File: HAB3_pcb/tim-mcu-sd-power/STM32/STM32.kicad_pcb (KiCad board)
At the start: 4 copper layers, 40 parts, among them J1 Conn_ARM_JTAG_SWD_20, J2 Micro_SD_Card_Det, J3 Conn_01x16_Male, J4 Conn_01x16_Male, J5 Conn_01x16_Male, J6 Conn_01x02_Male, J7 Conn_01x02_Male, J8 Conn_01x02_Male, J9 Conn_01x11_Male, SW1 SW_DPST_x2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

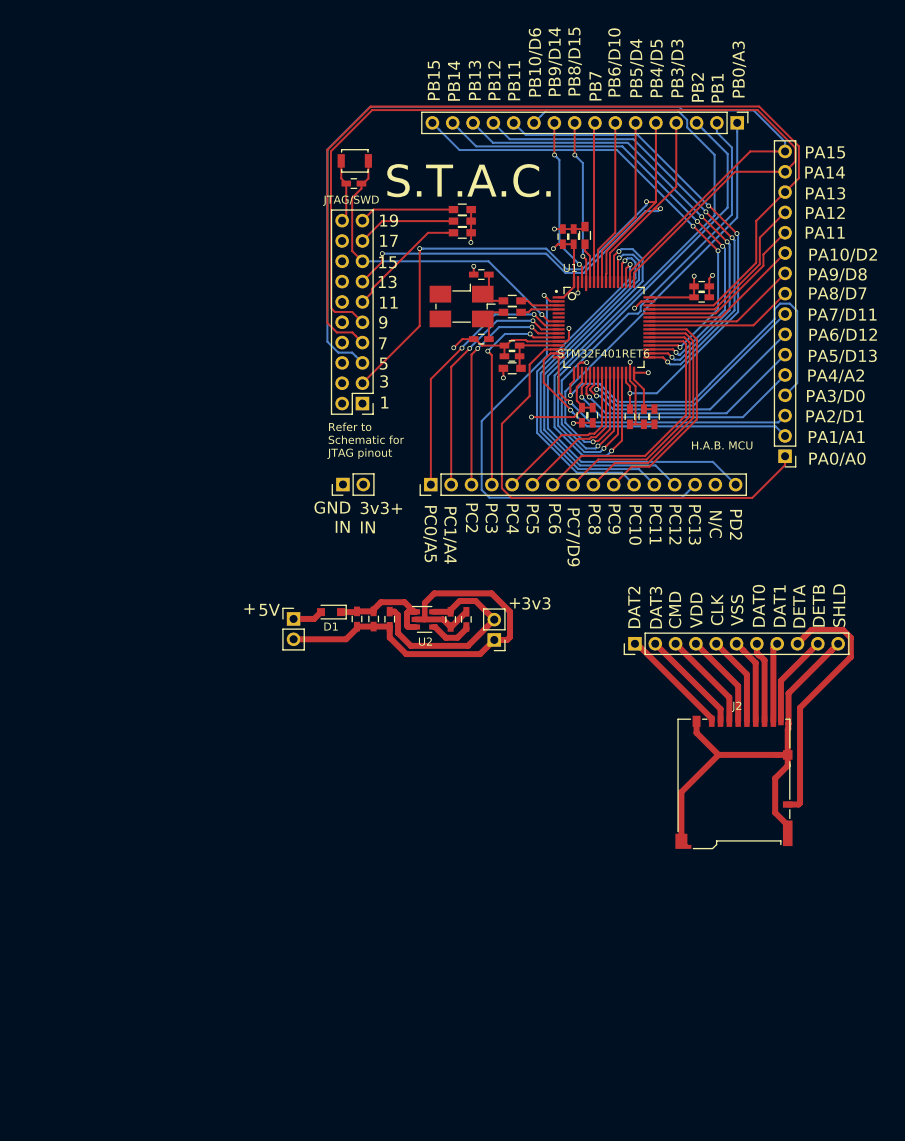
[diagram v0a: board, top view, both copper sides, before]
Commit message: Finished voltage regulator
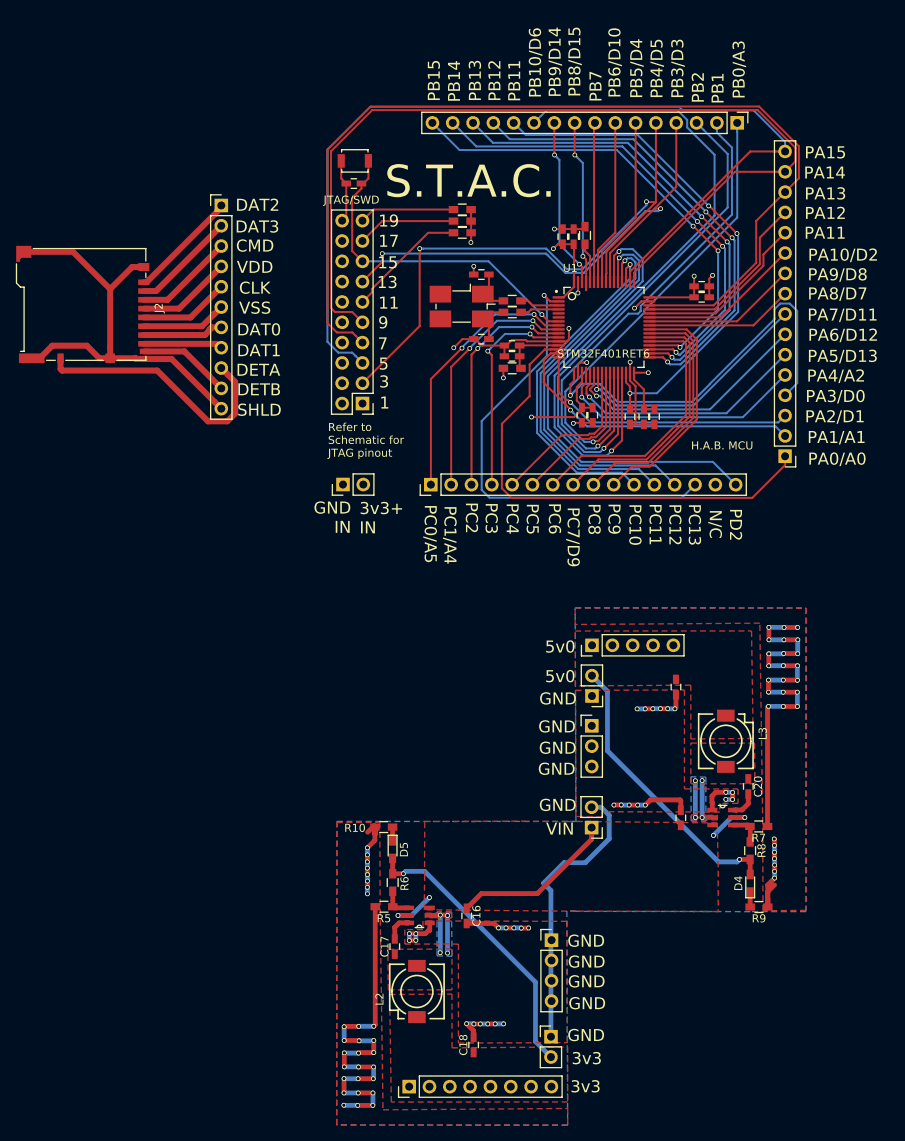
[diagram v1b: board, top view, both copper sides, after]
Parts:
- removed 100nF6: C17, Capacitors_SMD:C_0603_HandSoldering
- removed 100nF7: C20, Capacitors_SMD:C_0603_HandSoldering
- removed 10nF2: C18, Capacitors_SMD:C_0603_HandSoldering
- removed 1uF6: C16, Capacitors_SMD:C_0603_HandSoldering
- removed 1uF7: C19, Capacitors_SMD:C_0603_HandSoldering
- removed D1: D_Schottky, Diodes_SMD:D_SOD-323_HandSoldering
- added C16: 10uF, Capacitors_SMD:C_0603_HandSoldering, F.Cu at (131.3, 178.6)
- added C17: 100nF, Capacitors_SMD:C_0603_HandSoldering, F.Cu at (122.3, 182.4)
- added C18: 47uF, Capacitors_SMD:C_0603_HandSoldering, F.Cu at (132.2, 194.7)
- added C19: 10uF, Capacitors_SMD:C_0603_HandSoldering, F.Cu at (158.1, 166.3)
- added C20: 100nF, Capacitors_SMD:C_0603_HandSoldering, F.Cu at (166.5, 162.4)
- added C21: 47uF, Capacitors_SMD:C_0603_HandSoldering, F.Cu at (157.5, 150.0)
- added D4: LED, LEDs:LED_0603_HandSoldering, F.Cu at (166.8, 174.5)
- added D5: LED, LEDs:LED_0603_HandSoldering, F.Cu at (122.1, 170.3)
- added J10: Conn_01x02_Male, Pin_Headers:Pin_Header_Straight_1x02_Pitch2.54mm, F.Cu at (147.0, 151.1)
- added J12: Conn_01x03_Male, Pin_Headers:Pin_Header_Straight_1x03_Pitch2.54mm, F.Cu at (147.0, 154.8)
- added J13: Conn_01x04_Male, Pin_Headers:Pin_Header_Straight_1x04_Pitch2.54mm, F.Cu at (141.9, 181.6)
- added J14: Conn_01x05_Male, Pin_Headers:Pin_Header_Straight_1x05_Pitch2.54mm, F.Cu at (147.0, 144.7)
- added J15: Conn_01x08_Male, Pin_Headers:Pin_Header_Straight_1x08_Pitch2.54mm, F.Cu at (124.1, 199.9)
- added L2: 2.2uH, TPS564208:INDC7070X450, F.Cu at (125.0, 188.0)
- added L3: 3.3uH, TPS564208:INDC7070X450, F.Cu at (163.8, 156.8)
- added R10: 4.7k, Resistors_SMD:R_0603_HandSoldering, F.Cu at (121.0, 167.5)
- added R5: 10k, Resistors_SMD:R_0603_HandSoldering, F.Cu at (121.0, 177.4)
- added R6: 33.2k, Resistors_SMD:R_0603_HandSoldering, F.Cu at (122.1, 174.4)
- added R7: 10k, Resistors_SMD:R_0603_HandSoldering, F.Cu at (167.8, 167.4)
- added R8: 56.2k, Resistors_SMD:R_0603_HandSoldering, F.Cu at (166.8, 170.4)
- added R9: 4.7k, Resistors_SMD:R_0603_HandSoldering, F.Cu at (167.9, 177.5)
- added U3: TPS564208, TPS564208:TPS564208, F.Cu at (163.3, 166.3)
- 22uH1: value L -> L1
- U2: value LD3985M33R_SOT23 -> TPS564208; footprint TO_SOT_Packages_SMD:SOT-23-5 -> TPS564208:TPS564208
- moved J2 90.7 mm to (90.3, 99.4), turned to 270 degrees
- moved J9 75.3 mm to (100.7, 89.8), turned to 0 degrees
- moved J8 50.1 mm to (141.9, 193.7), turned to 0 degrees
- moved J7 45.5 mm to (147.0, 167.5), turned to 180 degrees
- moved U2 37.0 mm to (125.4, 178.5), turned to 180 degrees
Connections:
- J7 pad 1: Net-(D1-Pad2) -> Net-(C16-Pad1)
- J7 pad 2: Net-(100nF6-Pad1) -> Net-(C16-Pad2)
- J8 pad 1: Net-(100nF6-Pad1) -> Net-(C16-Pad2)
- J8 pad 2: Net-(100nF7-Pad2) -> Net-(C18-Pad1)
- U2 pad 1: Net-(100nF6-Pad2) -> Net-(C16-Pad2)
- U2 pad 2: Net-(100nF6-Pad1) -> Net-(C17-Pad1)
- U2 pad 3: Net-(100nF6-Pad2) -> Net-(C16-Pad1)
- U2 pad 5: Net-(100nF7-Pad2) -> Net-(C16-Pad1)
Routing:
- net Net-(C16-Pad2): track 0.00 -> 206.2 mm, vias 0 -> 87
- net Net-(100nF6-Pad1): track 56.0 -> 0.00 mm
- net Net-(C21-Pad1): track 0.00 -> 35.8 mm, vias 0 -> 1
- net Net-(C18-Pad1): track 0.00 -> 35.8 mm, vias 0 -> 1
- net Net-(C16-Pad1): track 0.00 -> 33.3 mm, vias 0 -> 4
- net Net-(100nF7-Pad2): track 26.8 -> 0.00 mm
- net Net-(100nF6-Pad2): track 14.4 -> 0.00 mm
- net Net-(C17-Pad1): track 0.00 -> 11.7 mm, vias 0 -> 4
- net Net-(C20-Pad1): track 0.00 -> 11.3 mm, vias 0 -> 4
- net Net-(R7-Pad2): track 0.00 -> 4.07 mm
- net Net-(C17-Pad2): track 0.00 -> 3.83 mm
- net Net-(D1-Pad2): track 3.78 -> 0.00 mm
- net Net-(C20-Pad2): track 0.00 -> 3.43 mm
- net Net-(D4-Pad1): track 0.00 -> 1.86 mm
- net Net-(D5-Pad1): track 0.00 -> 1.73 mm
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- added copper zone on F.Cu, net Net-(C16-Pad1)
- added copper zone on B.Cu, net Net-(C16-Pad2)
- added copper zone on F.Cu, net Net-(C16-Pad2)
- added copper zone on B.Cu, net Net-(C17-Pad1)
- added copper zone on F.Cu, net Net-(C17-Pad1)
- added copper zone on F.Cu, net Net-(C18-Pad1)
- added copper zone on B.Cu, net Net-(C20-Pad1)
- added copper zone on F.Cu, net Net-(C20-Pad1)
- added copper zone on F.Cu, net Net-(C21-Pad1)
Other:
- net class Default: trace_width 0.25 -> 0.6
- board text added: "5v0"
- board text added: "GND"
- board text added: "VIN"
- board text removed: "+"
- board text removed: "5V"

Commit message: final pcb designs complete
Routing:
- net +3V3: track 41.9 -> 84.7 mm, vias 5 -> 10
- net GND: track 58.0 -> 83.0 mm, vias 11 -> 17
- net (no net): track 0.00 -> 6.48 mm, vias 0 -> 2
- net PC12: track 54.3 -> 51.2 mm
- added copper zone on B.Cu, net +3V3
- added copper zone on F.Cu, net GND
- removed copper zone on In2.Cu, net +3V3
- removed copper zone on In1.Cu, net GND
